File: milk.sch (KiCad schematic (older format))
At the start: 5 parts, among them J1 RGB, J4 RST, K1 KEYSW, K2 KEYSW, U1 ProMicro

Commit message: initial schematic and layout (fails drc)
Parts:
- removed K1, K2: KEYSW, MX_Alps_Hybrid:MX-1U-NoLED, symbol milk-rescue:KEYSW-keyboard_parts
- removed U1: ProMicro, keyboard_parts:ProMicro_NoSilk, symbol promicro:ProMicro
- added C1: 0.1uf, Capacitor_SMD:C_0805_2012Metric_Pad1.18x1.45mm_HandSolder, symbol Device:C
- added D1, D2: 3.6V, Diode_SMD:D_SOD-123, symbol Diode:BZT52Bxx
- added F1: Polyfuse, Resistor_SMD:R_1206_3216Metric_Pad1.30x1.75mm_HandSolder, symbol Device:Polyfuse
- added J1: USB_C_Receptacle_USB2.0, footprints:Molex_2171800001, symbol Connector:USB_C_Receptacle_USB2.0
- added R1, R2: 5.1K, Resistor_SMD:R_0805_2012Metric_Pad1.20x1.40mm_HandSolder, symbol Device:R
- added R3, R4: 68, Resistor_SMD:R_0805_2012Metric_Pad1.20x1.40mm_HandSolder, symbol Device:R
- added R5: 1.5K, Resistor_SMD:R_0805_2012Metric_Pad1.20x1.40mm_HandSolder, symbol Device:R
- added SW1, SW2: SW_Push, Button_Switch_Keyboard:SW_Cherry_MX_1.00u_PCB, symbol Switch:SW_Push
- added U1: ATtiny85-20SU, Package_SO:SOIJ-8_5.3x5.3mm_P1.27mm, symbol MCU_Microchip_ATtiny:ATtiny85-20SU
- renumbered J4 to J2, J1 to J3
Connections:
- net labels added: +5V, D+, D-, PB3, PB4
- net labels removed: RA1, RB1, k1, k2
- wire segments 6 -> 35
- no-connect marks 0 -> 2
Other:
- moved on the sheet: J2, J3

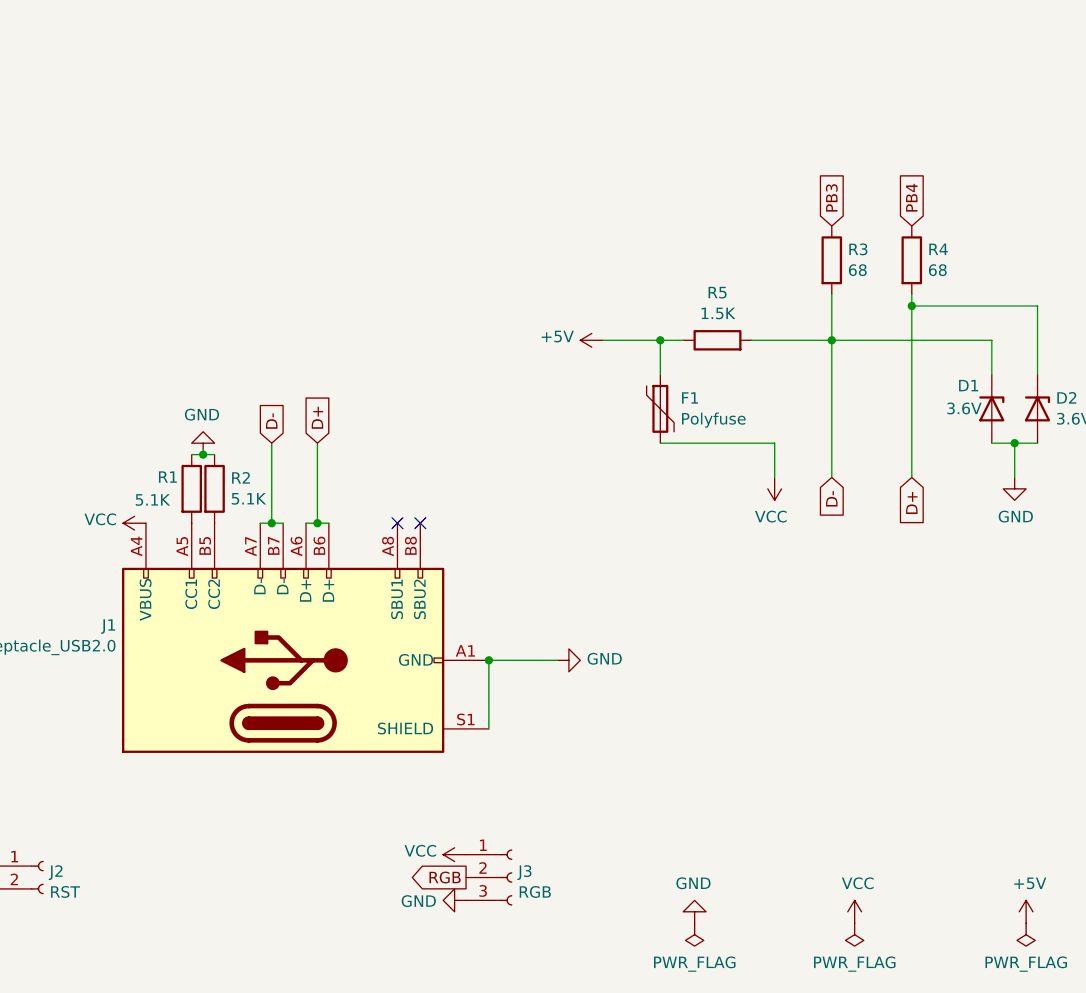
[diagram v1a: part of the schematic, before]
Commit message: Add programming headers (all over the place... yes)
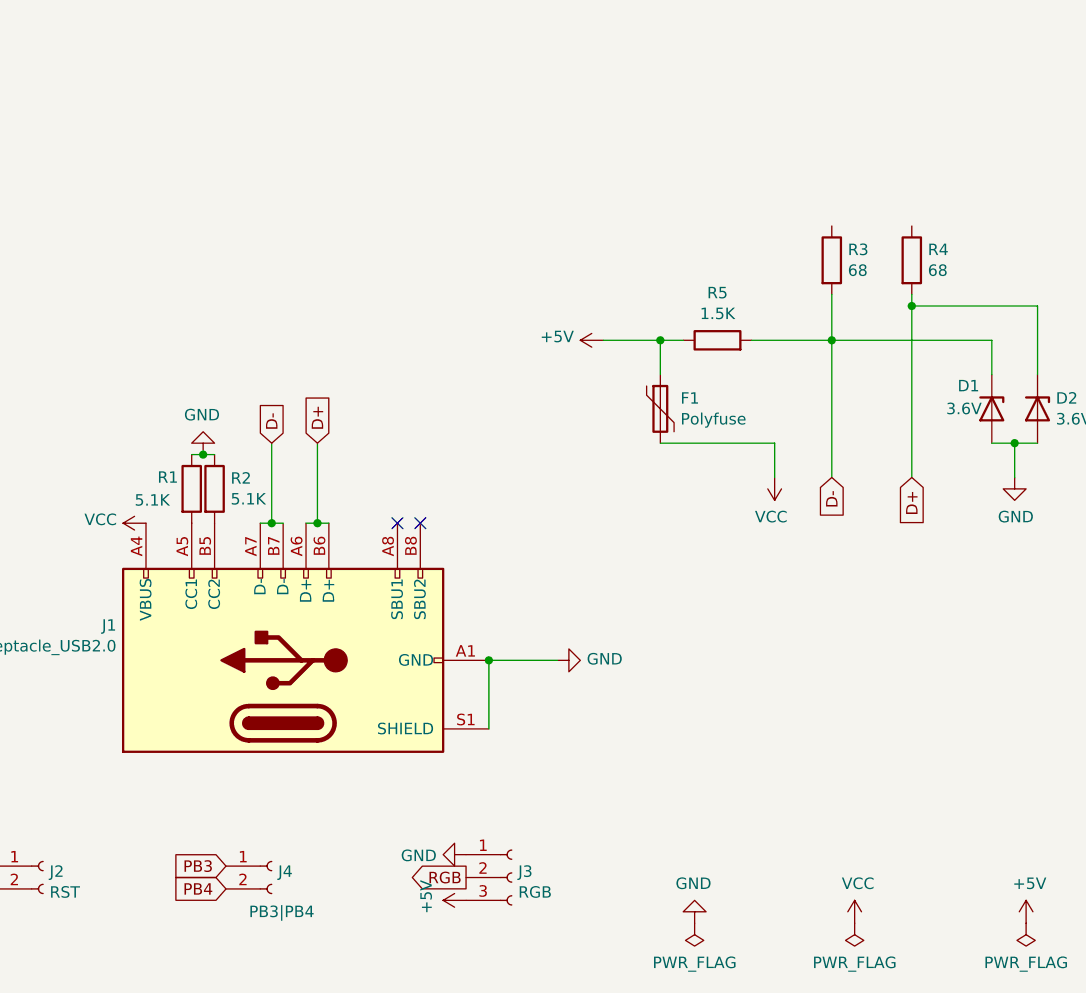
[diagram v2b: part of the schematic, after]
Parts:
- added J4: PB3|PB4, Connector_PinHeader_2.54mm:PinHeader_1x02_P2.54mm_Vertical, symbol Connector:Conn_01x02_Female
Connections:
- net +5V: now also J3.3 (Pin_3)
- net GND: now also J3.1 (Pin_1); no longer J3.3 (Pin_3)
- net PB3: now also J4.1 (Pin_1); no longer R3.1
- net PB4: now also J4.2 (Pin_2); no longer R4.1
- net VCC: no longer J3.1 (Pin_1)
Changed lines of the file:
@@
 L power:GND #PWR0108
 U 1 1 612C55C1
-P 3300 7050
-F 0 "#PWR0108" H 3300 6800 50  0001 C CNN
-F 1 "GND" V 3305 6922 50  0000 R CNN
-F 2 "" H 3300 7050 50  0001 C CNN
-F 3 "" H 3300 7050 50  0001 C CNN
-	1    3300 7050
+P 3300 6850
+F 0 "#PWR0108" H 3300 6600 50  0001 C CNN
+F 1 "GND" V 3305 6722 50  0000 R CNN
+F 2 "" H 3300 6850 50  0001 C CNN
+F 3 "" H 3300 6850 50  0001 C CNN
+	1    3300 6850
 	0    1    1    0
 $EndComp
@@
 Text GLabel 3300 6950 0    50   Output ~ 0
 RGB
-$Comp
-L power:VCC #PWR0109
-U 1 1 612C65E7
-P 3300 6850
-F 0 "#PWR0109" H 3300 6700 50  0001 C CNN
-F 1 "VCC" V 3315 6977 50  0000 L CNN
-F 2 "" H 3300 6850 50  0001 C CNN
-F 3 "" H 3300 6850 50  0001 C CNN
-	1    3300 6850
-	0    -1   -1   0
-$EndComp
 $Comp
 L power:VCC #PWR0110
@@
 	4250 4600 4150 4600
 Connection ~ 4150 4600
-Text GLabel 4900 4100 1    50   Input ~ 0
+Text GLabel 2250 6900 0    50   Input ~ 0
 PB3
-Text GLabel 5250 4100 1    50   Input ~ 0
+Text GLabel 2250 7000 0    50   Input ~ 0
 PB4
 Wire Wire Line
@@
 	1    0    0    -1
 $EndComp
+$Comp
+L power:+5V #PWR?
+U 1 1 6129FB48
+P 3300 7050
+F 0 "#PWR?" H 3300 6900 50  0001 C CNN
+F 1 "+5V" H 3315 7223 50  0000 C CNN
+F 2 "" H 3300 7050 50  0001 C CNN
+F 3 "" H 3300 7050 50  0001 C CNN
+	1    3300 7050
+	0    -1   -1   0
+$EndComp
+$Comp
+L Connector:Conn_01x02_Female J4
+U 1 1 612A3118
+P 2450 6900
+F 0 "J4" H 2478 6876 50  0000 L CNN
+F 1 "PB3|PB4" H 2350 6700 50  0000 L CNN
+F 2 "Connector_PinHeader_2.54mm:PinHeader_1x02_P2.54mm_Vertical" H 2450 6900 50  0001 C CNN
+F 3 "~" H 2450 6900 50  0001 C CNN
+	1    2450 6900
+	1    0    0    -1
+$EndComp

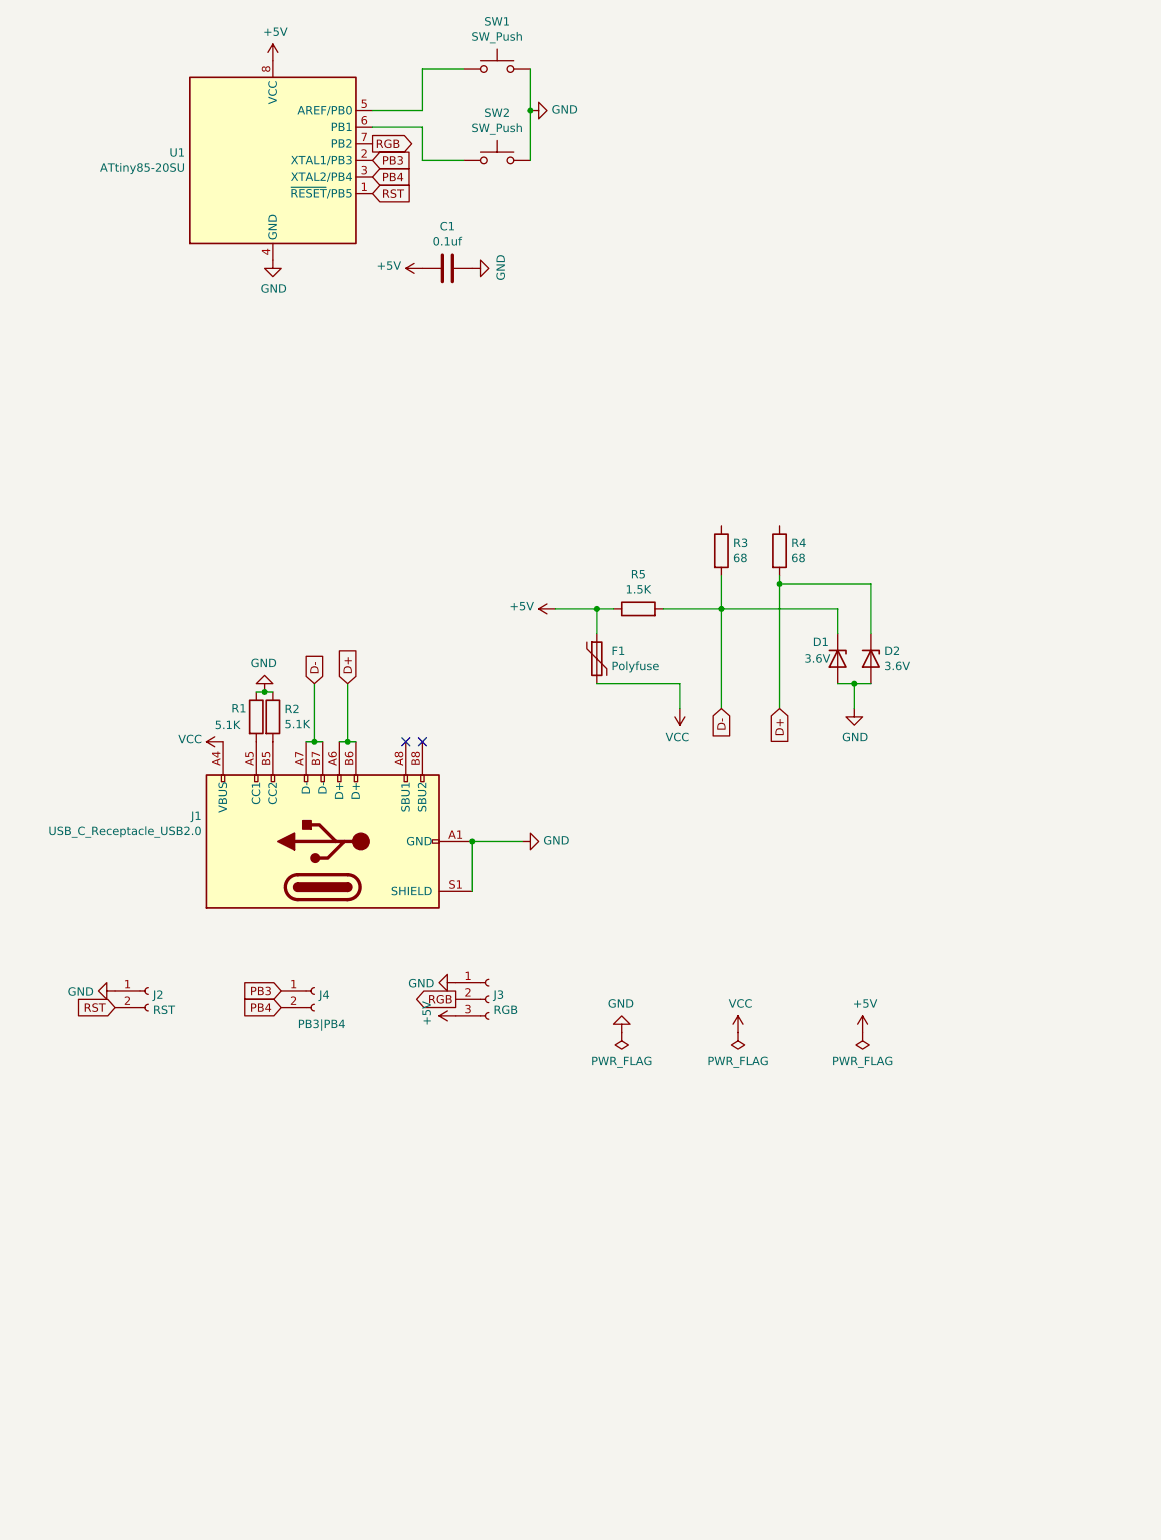
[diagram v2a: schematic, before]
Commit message: Fix pogo pin tht holes
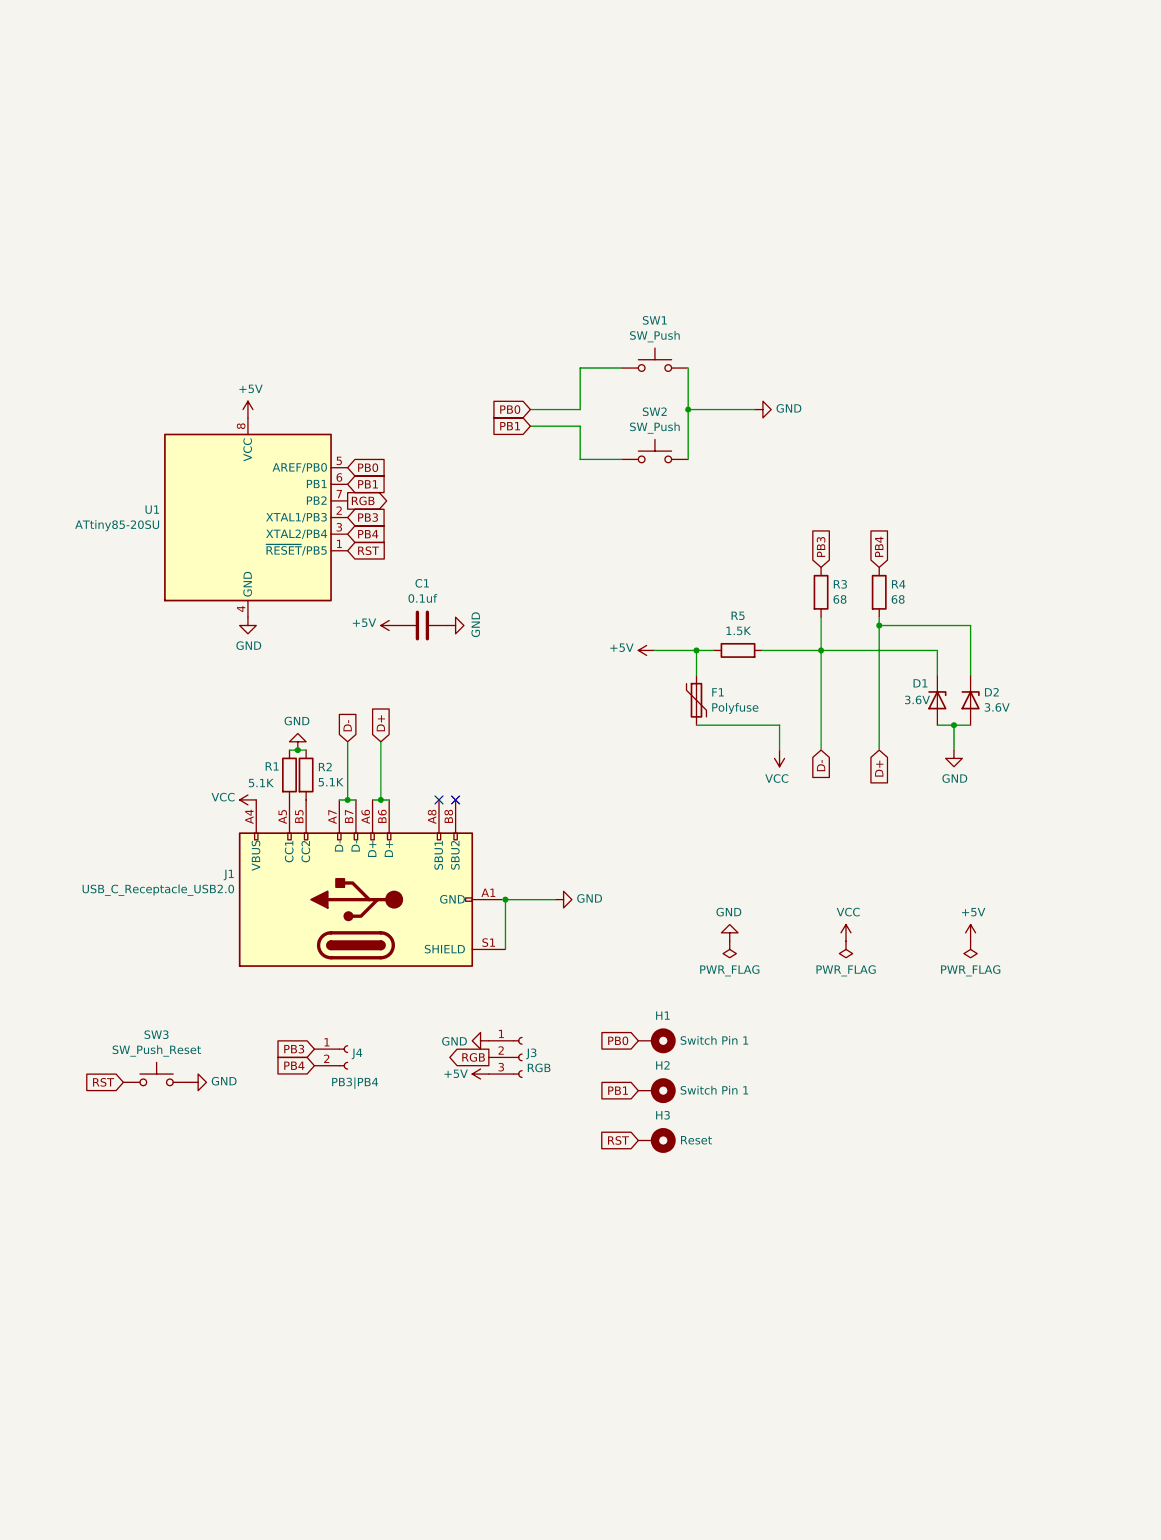
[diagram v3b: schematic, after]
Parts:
- removed J2: RST, Connector_PinHeader_2.54mm:PinHeader_1x02_P2.54mm_Vertical, symbol Connector:Conn_01x02_Female
- added H1, H2: Switch Pin 1, TestPoint:TestPoint_THTPad_D1.5mm_Drill0.7mm, symbol Mechanical:MountingHole_Pad
- added H3: Reset, TestPoint:TestPoint_THTPad_D1.5mm_Drill0.7mm, symbol Mechanical:MountingHole_Pad
- added SW3: SW_Push_Reset, footprints:ResetSW_1side, symbol Switch:SW_Push
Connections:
- net GND: now also SW3.2
- net PB3: now also R3.1
- net PB4: now also R4.1
- net RST: now also H3.1, SW3.1
- net PB0: now reaches SW1.1, U1.5 (AREF/PB0)
- net PB0: now also H1.1
- net PB1: now reaches SW2.1, U1.6 (PB1)
- net PB1: now also H2.1
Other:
- moved on the sheet: C1, D1, D2, F1, J1, J3, J4, R1, R2, R3, R4, R5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

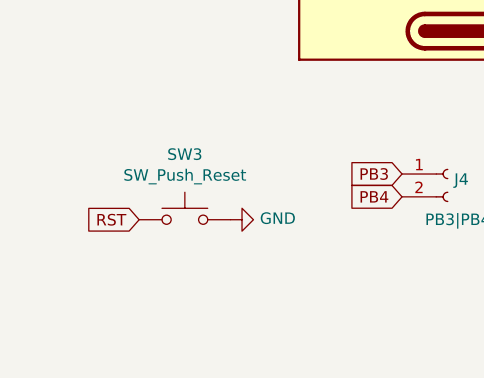
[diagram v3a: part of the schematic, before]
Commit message: Add pull up resistor for Reset/PB5
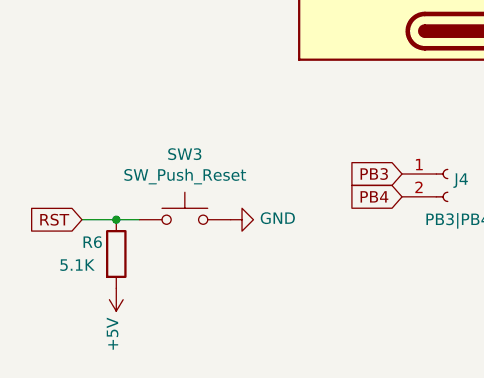
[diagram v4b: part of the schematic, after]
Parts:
- added R6: 5.1K, Resistor_SMD:R_0805_2012Metric_Pad1.20x1.40mm_HandSolder, symbol Device:R
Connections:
- net +5V: now also R6.2
- net RST: now also R6.1
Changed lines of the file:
@@
 	0    -1   -1   0
 $EndComp
-Text GLabel 1300 7450 0    50   Input ~ 0
+Text GLabel 1050 7450 0    50   Input ~ 0
 RST
 $Comp
@@
 Text GLabel 4400 7800 0    50   Input ~ 0
 RST
+Wire Wire Line
+	1050 7450 1200 7450
+$Comp
+L Device:R R6
+U 1 1 612BC4CA
+P 1200 7600
+F 0 "R6" H 1050 7650 50  0000 L CNN
+F 1 "5.1K" H 950 7550 50  0000 L CNN
+F 2 "Resistor_SMD:R_0805_2012Metric_Pad1.20x1.40mm_HandSolder" V 1130 7600 50  0001 C CNN
+F 3 "~" H 1200 7600 50  0001 C CNN
+	1    1200 7600
+	1    0    0    -1
+$EndComp
+Connection ~ 1200 7450
+Wire Wire Line
+	1200 7450 1300 7450
+$Comp
+L power:+5V #PWR0118
+U 1 1 612BCE38
+P 1200 7750
+F 0 "#PWR0118" H 1200 7600 50  0001 C CNN
+F 1 "+5V" V 1215 7878 50  0000 L CNN
+F 2 "" H 1200 7750 50  0001 C CNN
+F 3 "" H 1200 7750 50  0001 C CNN
+	1    1200 7750
+	-1   0    0    1
+$EndComp
 $EndSCHEMATC
